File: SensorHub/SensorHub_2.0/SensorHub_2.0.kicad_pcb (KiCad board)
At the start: 2 copper layers, 1 part, among them U1 R7FA4E2B93CFM#AA0

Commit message: 1st version SensorHub
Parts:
- added C1: 10 uF, Capacitor_SMD:C_0603_1608Metric, F.Cu at (200.5, 120.0)
- added C10: 4.7 uF, Capacitor_SMD:C_0603_1608Metric, F.Cu at (184.0, 113.5)
- added C11: 0.1 uF, Capacitor_SMD:C_0603_1608Metric, F.Cu at (195.9, 106.5)
- added C12: 0.1 uF, Capacitor_SMD:C_0603_1608Metric, F.Cu at (183.3, 118.5)
- added C2: 10 uF, Capacitor_SMD:C_0603_1608Metric, F.Cu at (196.0, 120.0)
- added C3: 1 milF, Capacitor_SMD:C_0603_1608Metric, F.Cu at (199.0, 120.0)
- added C4: 1 milF, Capacitor_SMD:C_0603_1608Metric, F.Cu at (194.5, 120.0)
- added C5: 1 uF, Capacitor_SMD:C_0603_1608Metric, F.Cu at (196.0, 103.5)
- added C6: 0.1 uF, Capacitor_SMD:C_0603_1608Metric, F.Cu at (197.5, 120.0)
- added C7: 1 uF, Capacitor_SMD:C_0603_1608Metric, F.Cu at (178.7, 100.5)
- added C8: 0.1 uF, Capacitor_SMD:C_0603_1608Metric, F.Cu at (195.5, 113.0)
- added C9: 0.1 uF, Capacitor_SMD:C_0603_1608Metric, F.Cu at (194.0, 113.0)
- added D1: LED, LED_SMD:LED_0402_1005Metric, F.Cu at (188.7, 96.0)
- added D2: LED, LED_SMD:LED_0402_1005Metric, F.Cu at (186.1, 96.0)
- added D3: 1N4148WT, Diode_SMD:D_SOD-523, F.Cu at (200.0, 98.0)
- added F1: 6V 0.5A, SensorHub MicroMod Carrier v1.1.0b:0805, F.Cu at (204.5, 111.0)
- added J1: USB_B_Micro, Connector_USB:USB_Micro-B_Molex-105017-0001, F.Cu at (203.0, 103.8)
- added J2: Conn_01x03, Connector_PinHeader_2.54mm:PinHeader_1x03_P2.54mm_Vertical, F.Cu at (186.5, 120.5)
- added J3: Conn_01x05, Connector_PinHeader_2.54mm:PinHeader_1x05_P2.54mm_Vertical, F.Cu at (186.5, 116.7)
- added JP1: SolderJumper_3_Open, Jumper:SolderJumper-3_P1.3mm_Open_RoundedPad1.0x1.5mm, F.Cu at (198.0, 102.6)
- added JP2: SolderJumper_3_Open, Jumper:SolderJumper-3_P1.3mm_Open_RoundedPad1.0x1.5mm, F.Cu at (198.0, 107.3)
- added JP3: SolderJumper_3_Open, Jumper:SolderJumper-3_P1.3mm_Open_RoundedPad1.0x1.5mm, F.Cu at (198.0, 97.9)
- added R1: 15 K, Resistor_SMD:R_0201_0603Metric, F.Cu at (195.5, 100.5)
- added R10: 4.7 K, Resistor_SMD:R_0201_0603Metric, F.Cu at (187.5, 112.3)
- added R11: 1 K, Resistor_SMD:R_0201_0603Metric, F.Cu at (183.2, 117.0)
- added R2: 30 K, Resistor_SMD:R_0201_0603Metric, F.Cu at (196.3, 100.5)
- added R3: 1.33 K, Resistor_SMD:R_0201_0603Metric, F.Cu at (190.6, 96.0)
- added R4: 4.7 K, Resistor_SMD:R_0201_0603Metric, F.Cu at (177.5, 102.9)
- added R5: 1.5 K, Resistor_SMD:R_0201_0603Metric, F.Cu at (177.5, 107.4)
- added R6: 10 K, Resistor_SMD:R_0201_0603Metric, F.Cu at (177.5, 104.4)
- added R7: ~, Resistor_SMD:R_0201_0603Metric, F.Cu at (200.0, 103.8)
- added R8: 1.33 K, Resistor_SMD:R_0201_0603Metric, F.Cu at (184.4, 96.0)
- added R9: 4.7 K, Resistor_SMD:R_0201_0603Metric, F.Cu at (188.2, 112.3)
- added S1: Reset, Library:Button_Mini_2.5x1.7mm, F.Cu at (178.5, 103.4)
- added S2: Boot, Library:Button_Mini_2.5x1.7mm, F.Cu at (178.5, 107.5)
- added U$40: ROBOTPATIENT_SMALL_MODULEBOARD, RobotPatient_BMI270_v1.2_Feb2024:RP_SMALL_SENSOR_OUTLINE, F.Cu at (191.5, 109.0)
- added U2: AP2112K-3.3, Package_TO_SOT_SMD:SOT-23-5, F.Cu at (204.1, 116.5)
- added U3: TJA1051TK-3, Package_SON:HVSON-8-1EP_3x3mm_P0.65mm_EP1.6x2.4mm, F.Cu at (201.5, 112.0)
- added U4: BMI270, BMI270:XDCR_BMI270, F.Cu at (191.0, 113.0)
- moved U1 68.4 mm to (187.8, 104.2), turned to 90 degrees
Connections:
- U1 pad 1: unconnected-(U1-P400-Pad1) -> /Sleep
- U1 pad 11: unconnected-(U1-VCC-Pad11) -> +3.3V
- U1 pad 15: unconnected-(U1-P408-Pad15) -> /SCX
- U1 pad 16: unconnected-(U1-P407-Pad16) -> /SDX
- U1 pad 17: unconnected-(U1-VSS_USB-Pad17) -> GND
- U1 pad 18: unconnected-(U1-USB_DM-Pad18) -> /USB_DM
- U1 pad 19: unconnected-(U1-USB_DP-Pad19) -> /USB_DP
- U1 pad 2: unconnected-(U1-P401-Pad2) -> /TXD
- U1 pad 20: unconnected-(U1-VCC_USB-Pad20) -> /V_USB_Mic
- U1 pad 25: unconnected-(U1-~{RES}-Pad25) -> /RES
- U1 pad 26: unconnected-(U1-MD-Pad26) -> /Boot
- U1 pad 3: unconnected-(U1-CACREF-Pad3) -> /RXD
- U1 pad 37: unconnected-(U1-P112-Pad37) -> /P112
- U1 pad 38: unconnected-(U1-P113-Pad38) -> /P113
- U1 pad 39: unconnected-(U1-VCC-Pad39) -> +3.3V
- U1 pad 40: unconnected-(U1-VSS-Pad40) -> GND
- U1 pad 44: unconnected-(U1-P104-Pad44) -> /INT1
- U1 pad 5: unconnected-(U1-VCL-Pad5) -> /VCL
- U1 pad 56: unconnected-(U1-VREFH-Pad56) -> +3.3V
- U1 pad 59: unconnected-(U1-VREFH0-Pad59) -> +3.3V
- U1 pad 64: unconnected-(U1-P000-Pad64) -> /P000
- U1 pad 8: unconnected-(U1-VSS-Pad8) -> GND
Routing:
- net GND: track 0.00 -> 147.5 mm, vias 0 -> 15
- net +3.3V: track 0.00 -> 87.1 mm, vias 0 -> 8
- net +5V: track 0.00 -> 29.9 mm
- net /RES: track 0.00 -> 22.8 mm, vias 0 -> 2
- net /RXD: track 0.00 -> 21.3 mm, vias 0 -> 2
- net /INT1: track 0.00 -> 21.0 mm
- net /TXD: track 0.00 -> 19.2 mm
- net /SCX: track 0.00 -> 19.1 mm
- net /Sleep: track 0.00 -> 18.8 mm
- net /Boot: track 0.00 -> 18.7 mm, vias 0 -> 2
- net /SDX: track 0.00 -> 18.2 mm, vias 0 -> 3
- net Net-(D3-K): track 0.00 -> 13.5 mm
- net /V_usb: track 0.00 -> 12.9 mm
- net /P000: track 0.00 -> 9.65 mm
- net /V_USB_Mic: track 0.00 -> 8.91 mm
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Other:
- board outline added: 30 x 28 mm

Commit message: MYRGM080200C41RA
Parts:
- removed J1: USB_B_Micro, Connector_USB:USB_Micro-B_Molex-105017-0001
- removed JP1, JP2, JP3: SolderJumper_3_Open, Jumper:SolderJumper-3_P1.3mm_Open_RoundedPad1.0x1.5mm
- removed R7: ~, Resistor_SMD:R_0201_0603Metric
- added C13: 0.1 uF, Capacitor_SMD:C_0603_1608Metric, F.Cu at (159.9, 111.0)
- added C14: 0.1 uF, Capacitor_SMD:C_0603_1608Metric, F.Cu at (159.9, 113.5)
- added C15: 0.1 uF, Capacitor_SMD:C_0603_1608Metric, F.Cu at (159.9, 116.0)
- added J4: USB_C_Receptacle, Connector_USB:USB_C_Receptacle_Molex_105450-0101, F.Cu at (130.1, 108.3)
- added R12: 15 K, Resistor_SMD:R_0201_0603Metric, F.Cu at (128.8, 118.9)
- added R13: ~, Resistor_SMD:R_0201_0603Metric, F.Cu at (113.9, 98.5)
- added R14: ~, Resistor_SMD:R_0201_0603Metric, F.Cu at (113.9, 100.2)
- C1, C2: value 10 uF -> 10V/22uF
- C3: value 1 milF -> 330 pF
- C4: value 1 milF -> 50 nF
- C5: value 1 uF -> 0.1 uF
- C6: value 0.1 uF -> 16V/1uF
- F1: footprint SensorHub MicroMod Carrier v1.1.0b:0805 -> Fuse:Fuse_1206_3216Metric_Pad1.42x1.75mm_HandSolder
- R1: value 15 K -> 10 K
- R2: value 30 K -> 47 K
- U2: value AP2112K-3.3 -> MYRGM080200C41RA; footprint Package_TO_SOT_SMD:SOT-23-5 -> MYRGM080200C41RA:MURATA_MYRGM080200C41RA_0
- moved F1 87.6 mm to (116.9, 113.2), turned to 0 degrees
- moved D3 85.9 mm to (116.2, 117.1), turned to 0 degrees
- moved C4 83.2 mm to (114.7, 96.4), turned to 0 degrees
- moved U2 73.1 mm to (131.1, 118.3)
- moved C7 72.4 mm to (106.5, 105.2), turned to 180 degrees
- moved S1 72.0 mm to (106.5, 106.6), turned to 0 degrees
- moved C3 71.4 mm to (127.6, 118.1)
- moved R1 70.6 mm to (127.6, 120.0), turned to 180 degrees
- moved R2 69.6 mm to (128.8, 117.4), turned to -90 degrees
- moved C1 69.4 mm to (131.2, 123.6), turned to 0 degrees
- moved C2 67.8 mm to (128.4, 115.2), turned to 90 degrees
- moved R4 67.1 mm to (110.5, 106.6), turned to 0 degrees
- moved C6 66.4 mm to (131.2, 122.1), turned to 0 degrees
- moved S2 59.5 mm to (119.2, 102.4), turned to 0 degrees
- moved R5 59.2 mm to (118.4, 104.4), turned to 0 degrees
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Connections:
- C11 pad 1: /V_USB_Mic -> +3.3V
- C3 pad 1: +5V -> +3.3V
- C3 pad 2: GND -> /FB
- C4 pad 1: +3.3V -> Net-(C4-Pad1)
- C5 pad 1: GND -> +3.3V
- C5 pad 2: /V_USB_Mic -> GND
- J2 pad 2: GND -> +3.3V
- J2 pad 3: +3.3V -> GND
- R1 pad 1: /V_USB_Mic -> /Sleep
- R1 pad 2: /V_USB_Mic_inp -> GND
- R2 pad 1: /V_USB_Mic -> +3.3V
- R2 pad 2: GND -> /FB
- U1 pad 1: /Sleep -> unconnected-(U1-P400-Pad1)
- U1 pad 20: /V_USB_Mic -> +3.3V
- U1 pad 34: unconnected-(U1-CLKOUT-Pad34) -> /P109 / TXD9
- U2 pad 1: +5V -> unconnected-(U2-1_NC-Pad1)
- U2 pad 2: GND -> /LX
- U2 pad 3: +5V -> /LX
- U2 pad 5: +3.3V -> /FB
- U3 pad 8: /Sleep -> unconnected-(U3-S-Pad8)
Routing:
- net GND: track 147.5 -> 49.4 mm, vias 15 -> 0
- net +3.3V: track 87.1 -> 27.6 mm, vias 8 -> 0
- net /RES: track 22.8 -> 0.00 mm, vias 2 -> 0
- net /RXD: track 21.3 -> 0.00 mm, vias 2 -> 0
- net /INT1: track 21.0 -> 0.00 mm
- net /TXD: track 19.2 -> 0.00 mm
- net /SCX: track 19.1 -> 0.00 mm
- net /Boot: track 18.7 -> 0.00 mm, vias 2 -> 0
- net /SDX: track 18.2 -> 0.00 mm, vias 3 -> 0
- net /Sleep: track 18.8 -> 1.77 mm
- net +5V: track 29.9 -> 13.3 mm
- net Net-(D3-K): track 13.5 -> 0.00 mm
- net /V_usb: track 12.9 -> 0.00 mm
- net /P000: track 9.65 -> 0.00 mm
- net /V_USB_Mic: track 8.91 -> 0.00 mm
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
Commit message: ASCODV-24.000MHZ-LR-T3
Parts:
- added C16: 0.1 uF, Capacitor_SMD:C_0603_1608Metric, F.Cu at (137.2, 94.1)
- added U5: ASCODV-24.000MHZ-LR-T3, Library:ASCODV-24.000MHZ-LR-T3, F.Cu at (135.8, 91.1)
- moved U3 3.42 mm to (156.2, 91.0)
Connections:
- U1 pad 10: unconnected-(U1-EXTAL-Pad10) -> /EXTAL

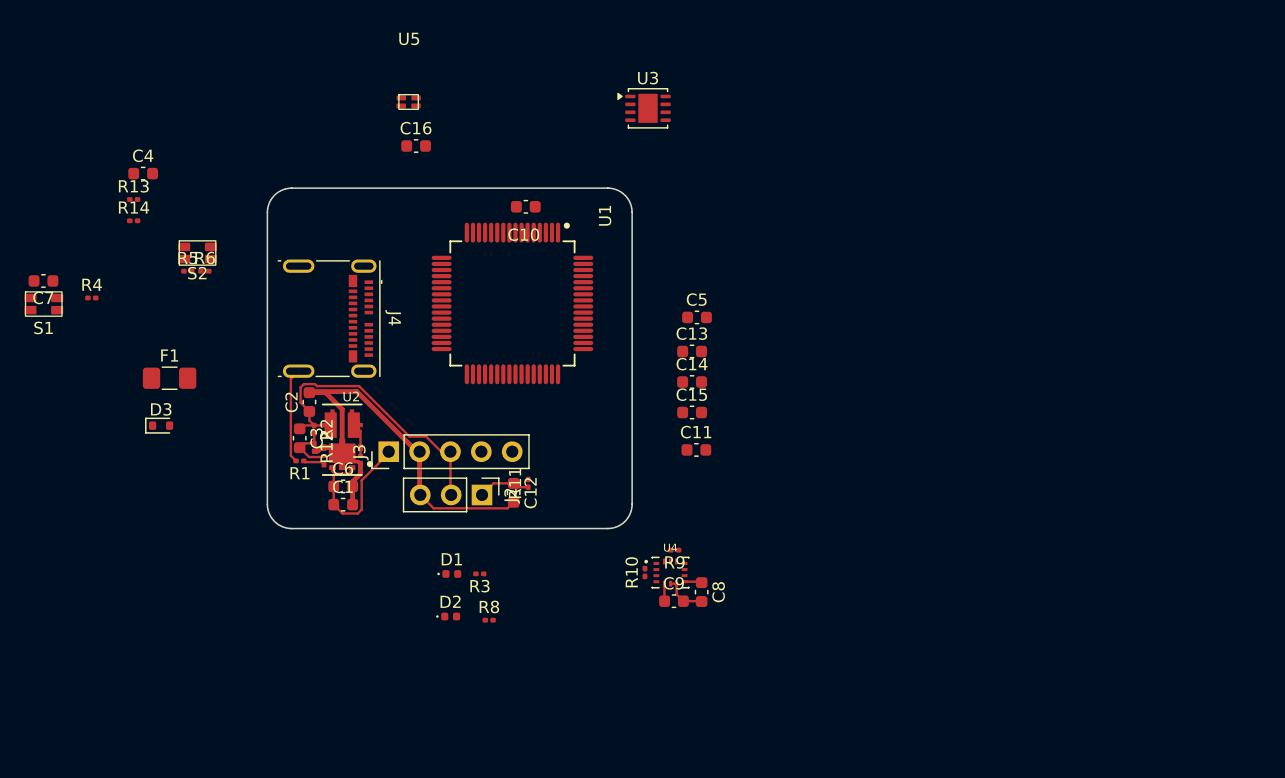
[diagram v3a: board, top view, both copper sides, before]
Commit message: New connector BM46B-12DP-0.35V(53)
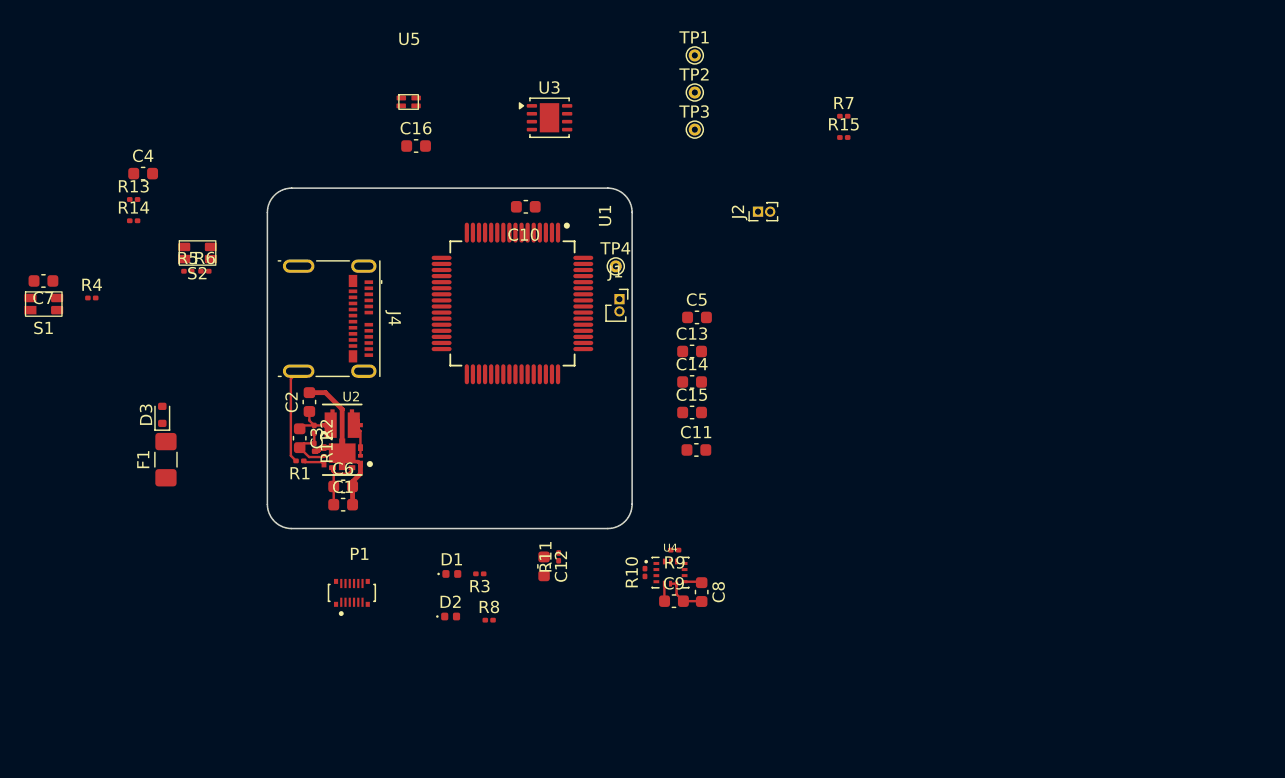
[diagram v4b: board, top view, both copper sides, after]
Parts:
- removed J3: Conn_01x05, Connector_PinHeader_2.54mm:PinHeader_1x05_P2.54mm_Vertical
- added J1: Conn_01x02, Connector_PinSocket_1.00mm:PinSocket_1x02_P1.00mm_Vertical, F.Cu at (153.9, 106.7)
- added P1: BM46B-12DP-0.35V_53_, BM46B-12DP-0.35V_53_:HRS_BM46B-12DP-0.35V_53_, F.Cu at (131.9, 130.9)
- added R15: 4.7 K, Resistor_SMD:R_0201_0603Metric, F.Cu at (172.4, 93.4)
- added R7: 4.7 K, Resistor_SMD:R_0201_0603Metric, F.Cu at (172.4, 91.7)
- added TP1: TestPoint, TestPoint:TestPoint_THTPad_D1.0mm_Drill0.5mm, F.Cu at (160.1, 86.7)
- added TP2: TestPoint, TestPoint:TestPoint_THTPad_D1.0mm_Drill0.5mm, F.Cu at (160.1, 89.7)
- added TP3: TestPoint, TestPoint:TestPoint_THTPad_D1.0mm_Drill0.5mm, F.Cu at (160.1, 92.8)
- added TP4: TestPoint, TestPoint:TestPoint_THTPad_D1.0mm_Drill0.5mm, F.Cu at (153.6, 104.0)
- J2: value Conn_01x03 -> Conn_01x02; footprint Connector_PinHeader_2.54mm:PinHeader_1x03_P2.54mm_Vertical -> Connector_PinHeader_1.00mm:PinHeader_1x02_P1.00mm_Vertical
- moved J2 32.5 mm to (165.3, 99.5), turned to 90 degrees
- moved U3 8.14 mm to (148.2, 91.8)
- moved F1 6.71 mm to (116.6, 119.9), turned to 90 degrees
- moved C12 6.55 mm to (147.7, 128.7)
- moved R11 6.55 mm to (148.9, 127.9)
- moved D3 0.89 mm to (116.3, 116.2), turned to 90 degrees
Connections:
- net /P000 renamed /ADC
- net V_Bus renamed /V_Bus
- J2 pad 1: /Analog -> GND
- J2 pad 2: +3.3V -> /TXD
- J4 pad A2: /P109 / TXD9 -> /SWDIO
- J4 pad B2: /P109 / TXD9 -> /SWDIO
- R10 pad 2: /SDX -> /MOSI/SDA
- R3 pad 1: /P112 -> /LED1
- R8 pad 1: /P113 -> /LED2
- R9 pad 2: /SCX -> /MISO/SCL
- U1 pad 1: unconnected-(U1-P400-Pad1) -> /INT2
- U1 pad 12: unconnected-(U1-P411-Pad12) -> /SWDIO
- U1 pad 14: unconnected-(U1-P409-Pad14) -> /GPIO
- U1 pad 15: /SCX -> unconnected-(U1-P408-Pad15)
- U1 pad 16: /SDX -> unconnected-(U1-P407-Pad16)
- U1 pad 2: /TXD -> /SCL_0
- U1 pad 22: unconnected-(U1-P206-Pad22) -> /LED2
- U1 pad 27: unconnected-(U1-P200-Pad27) -> /LED1
- U1 pad 28: unconnected-(U1-P304-Pad28) -> /INT2
- U1 pad 3: /RXD -> unconnected-(U1-CACREF-Pad3)
- U1 pad 32: unconnected-(U1-SWCLK-Pad32) -> GND
- U1 pad 33: unconnected-(U1-SWDIO-Pad33) -> /SWDIO
- U1 pad 34: /P109 / TXD9 -> /MISO/SCL
- U1 pad 35: unconnected-(U1-P110-Pad35) -> /MOSI/SDA
- U1 pad 36: unconnected-(U1-P111-Pad36) -> /SCK
- U1 pad 37: /P112 -> /CS
- U1 pad 38: /P113 -> unconnected-(U1-P113-Pad38)
- U1 pad 4: unconnected-(U1-P403-Pad4) -> /SDA_0
- U1 pad 47: unconnected-(U1-P101-Pad47) -> /SWDIO
- U1 pad 48: unconnected-(U1-P100-Pad48) -> /RXD
- U3 pad 1: /TXD -> /SWDIO
- U4 pad 13: /SCX -> /SCL_0
- U4 pad 14: /SDX -> /SDA_0
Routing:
- net GND: track 49.4 -> 26.5 mm
- net +3.3V: track 27.6 -> 6.97 mm
- net +5V: track 13.3 -> 4.89 mm
- net /Analog: track 4.32 -> 0.45 mm

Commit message: New testPoints and Res filter
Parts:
- removed J2: Conn_01x02, Connector_PinHeader_1.00mm:PinHeader_1x02_P1.00mm_Vertical
- added C17: 0.1 uF, Capacitor_SMD:C_0603_1608Metric, F.Cu at (124.0, 91.2)
- added R16: 1 K, Resistor_SMD:R_0201_0603Metric, F.Cu at (123.2, 92.3)
- added TP5: TestPoint, TestPoint:TestPoint_THTPad_D1.0mm_Drill0.5mm, F.Cu at (161.8, 87.5)
- added TP6: TestPoint, TestPoint:TestPoint_THTPad_D1.0mm_Drill0.5mm, F.Cu at (161.8, 90.6)
- added TP7: TestPoint, TestPoint:TestPoint_THTPad_D1.0mm_Drill0.5mm, F.Cu at (164.8, 87.5)
- added TP8: TestPoint, TestPoint:TestPoint_THTPad_D1.0mm_Drill0.5mm, F.Cu at (164.8, 90.6)
- moved TP4 14.4 mm to (158.8, 90.6)
- moved TP3 5.37 mm to (158.8, 87.5)
- moved TP1 4.49 mm to (155.7, 87.5)
- moved TP2 4.49 mm to (155.7, 90.6)
- moved J1 3.51 mm to (153.6, 103.2)
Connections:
- J1 pad 1: unconnected-(J1-Pin_1-Pad1) -> /SWDIO
- J1 pad 2: unconnected-(J1-Pin_2-Pad2) -> /SWCLK
- J4 pad A2: /SWDIO -> /TX+
- J4 pad A3: /RES -> /RES_usb
- J4 pad B2: /SWDIO -> /TX+
- J4 pad B3: /RES -> /RES_usb
- TP1 pad 1: GND -> +3.3V
- TP2 pad 1: GND -> /VCL
- TP3 pad 1: /SWDIO -> /SCL_0
- TP4 pad 1: /SWDIO -> /SDA_0
- U1 pad 12: /SWDIO -> /TX+
- U1 pad 32: GND -> /SWCLK
- U1 pad 47: /SWDIO -> /TX+
- U3 pad 1: /SWDIO -> /TX+

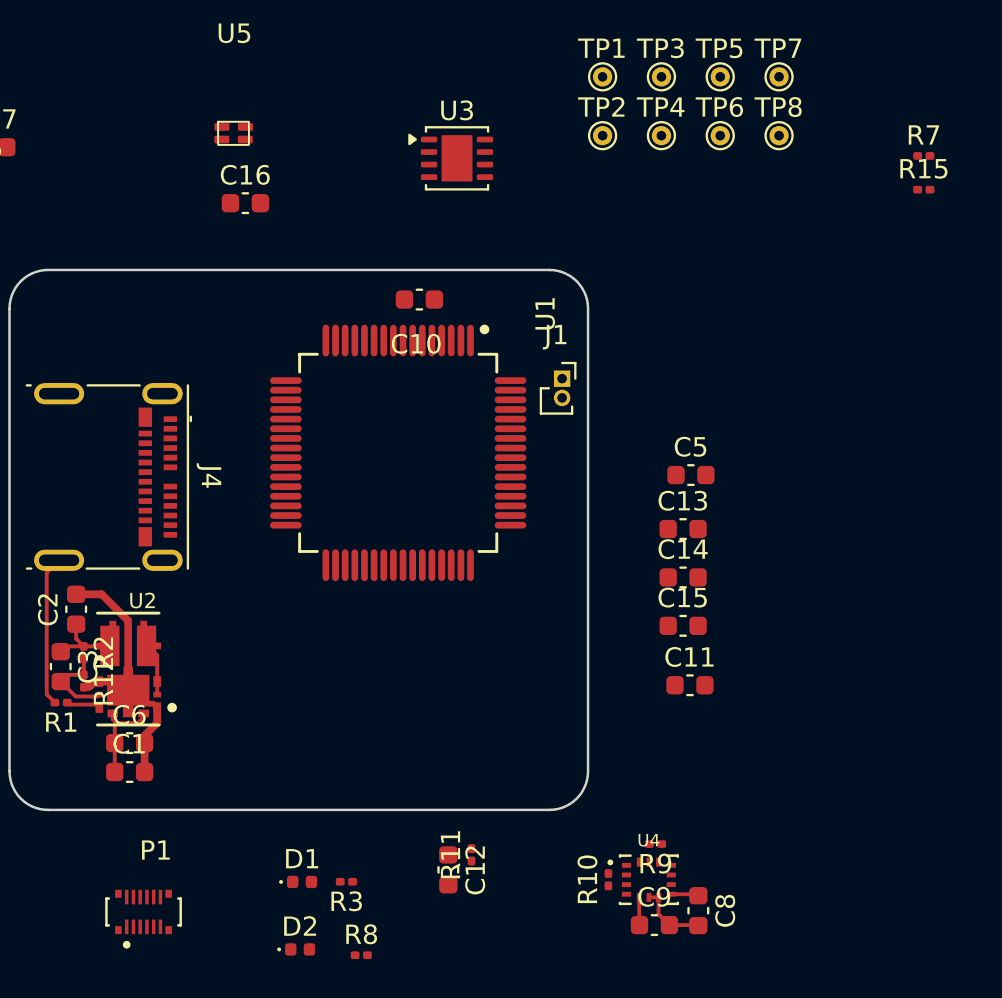
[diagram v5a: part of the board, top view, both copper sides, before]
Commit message: Mirrored connector
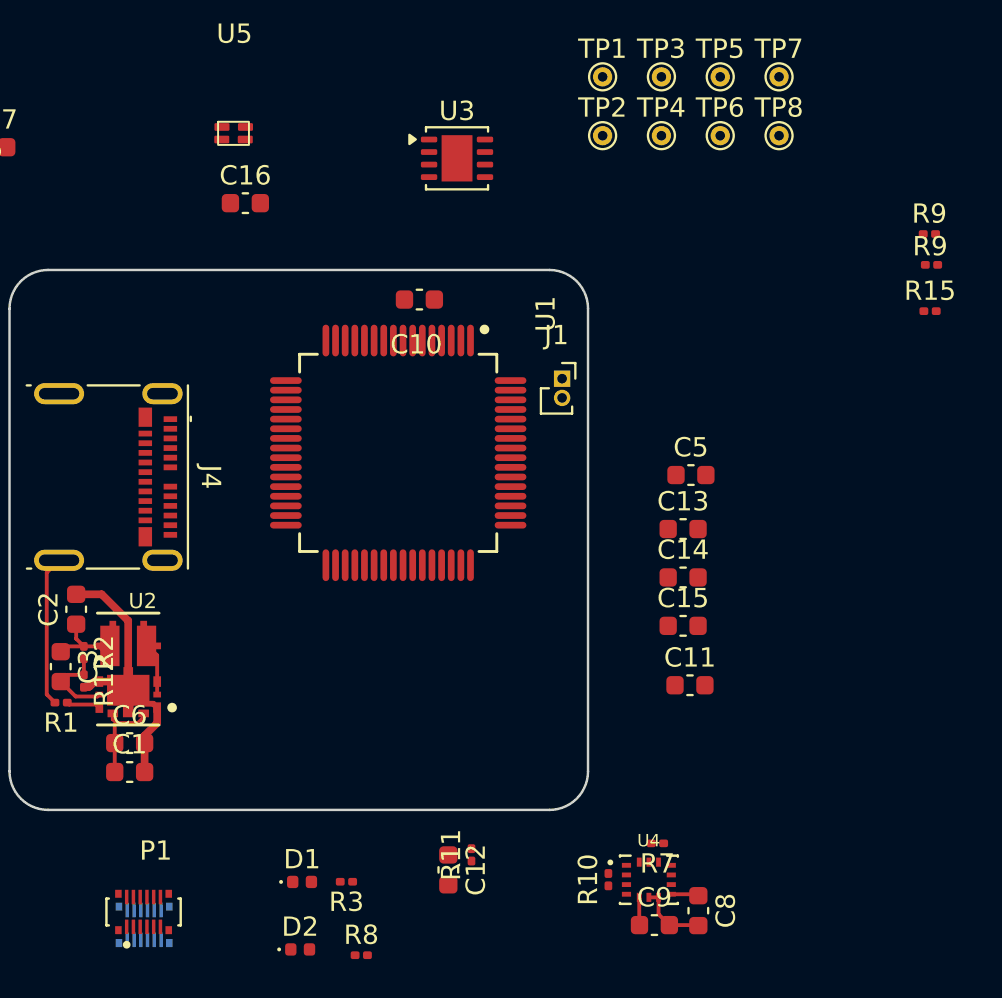
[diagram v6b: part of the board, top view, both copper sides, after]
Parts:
- added P2: BM46B-12DP-0.35V_53_, BM46B-12DP-0.35V_53_:HRS_BM46B-12DP-0.35V_53_, B.Cu at (131.9, 131.5)
- added R9: 4.7 K, Resistor_SMD:R_0201_0603Metric, F.Cu at (172.8, 97.3)
- moved R7 38.2 mm to (158.5, 127.3), turned to 180 degrees
- moved R9 34.7 mm to (172.6, 95.7), turned to 0 degrees
- moved R15 6.31 mm to (172.7, 99.7)

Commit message: Audio jumper
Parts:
- added C19: 1 uF, Capacitor_SMD:C_0603_1608Metric, F.Cu at (148.2, 134.6)
- added JP1: SolderJumper_2_Open, Jumper:SolderJumper-2_P1.3mm_Open_RoundedPad1.0x1.5mm, F.Cu at (152.2, 135.1)
- moved P2 3.86 mm to (129.4, 134.4)
- moved TP1 2.46 mm to (157.8, 88.8)
- moved TP2 2.46 mm to (157.8, 91.8)
- moved TP3 2.46 mm to (160.9, 88.8)
- moved TP4 2.46 mm to (160.9, 91.8)
- moved TP7 2.46 mm to (167.0, 88.8)
- moved TP8 2.46 mm to (167.0, 91.8)
- moved TP5 2.46 mm to (163.9, 88.8)
- moved TP6 2.46 mm to (163.9, 91.8)
- moved P1 1.23 mm to (130.7, 131.1)
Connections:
- C12 pad 2: GND -> Net-(JP1-B)
- R11 pad 2: /ADC -> Net-(C19-Pad2)
- U1 pad 53: unconnected-(U1-P014-Pad53) -> /ADC/DA
- U1 pad 64: /ADC -> unconnected-(U1-P000-Pad64)
